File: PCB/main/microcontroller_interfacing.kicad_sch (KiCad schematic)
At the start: 20 parts, among them U3 CH340G, U4 USB_Micro_B, U5 AT24C256C-SSHL-T, X1 12MHz Crystal

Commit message: Add USB footprint
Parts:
- U4: footprint Footprint_EEE3088F:MICRO-USB-SMD_U254-051T-4BH83-S1S -> Footprint_EEE3088F:C404969_Micro_USB
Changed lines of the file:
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@@
     (property "Reference" "U4" (id 0) (at 140.97 33.181 0))
     (property "Value" "USB_Micro_B" (id 1) (at 140.97 35.7179 0))
-    (property "Footprint" "Footprint_EEE3088F:MICRO-USB-SMD_U254-051T-4BH83-S1S" (id 2) (at 139.7 43.18 0)
+    (property "Footprint" "Footprint_EEE3088F:C404969_Micro_USB" (id 2) (at 139.7 43.18 0)
       (effects (font (size 1.27 1.27)) hide)
     )

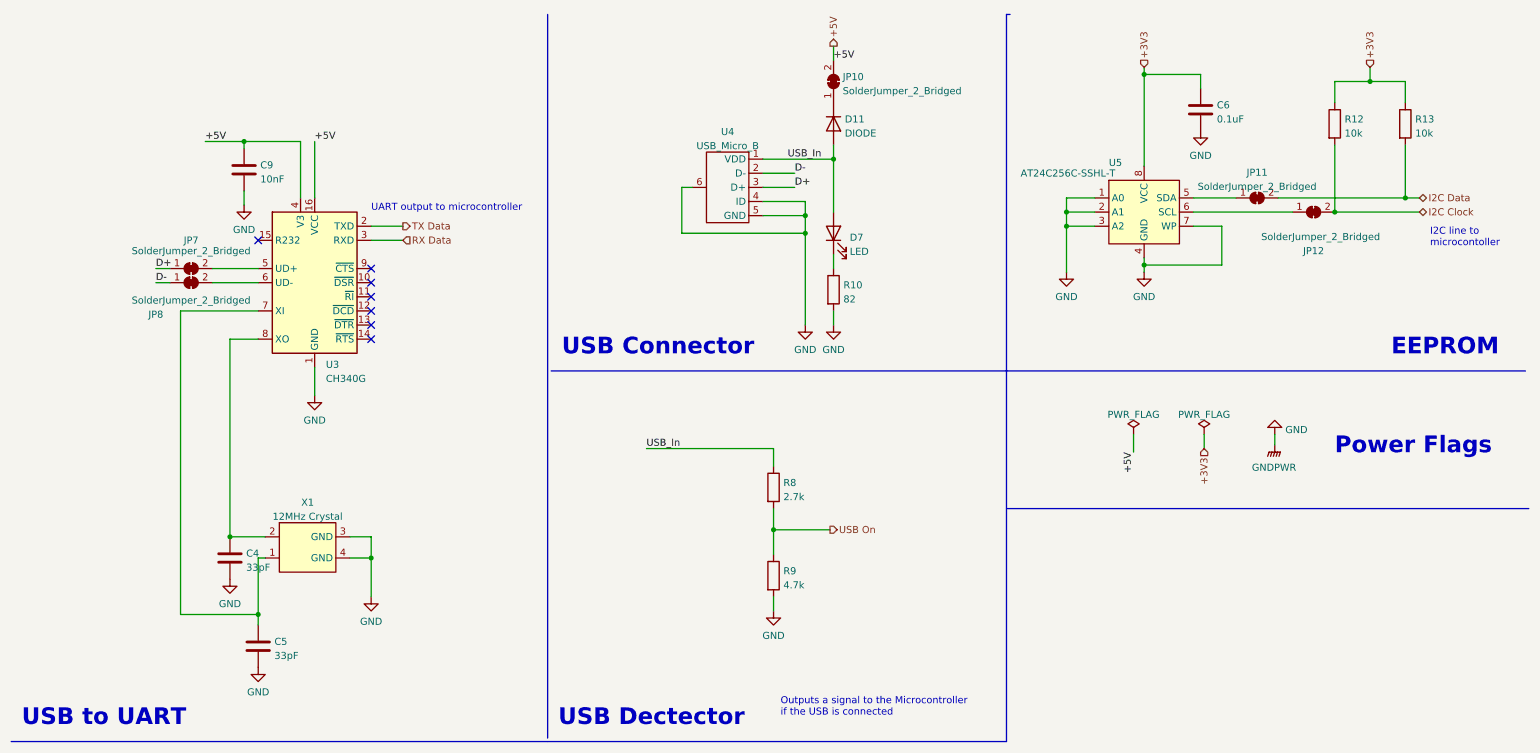
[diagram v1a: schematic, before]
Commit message: Add footprints
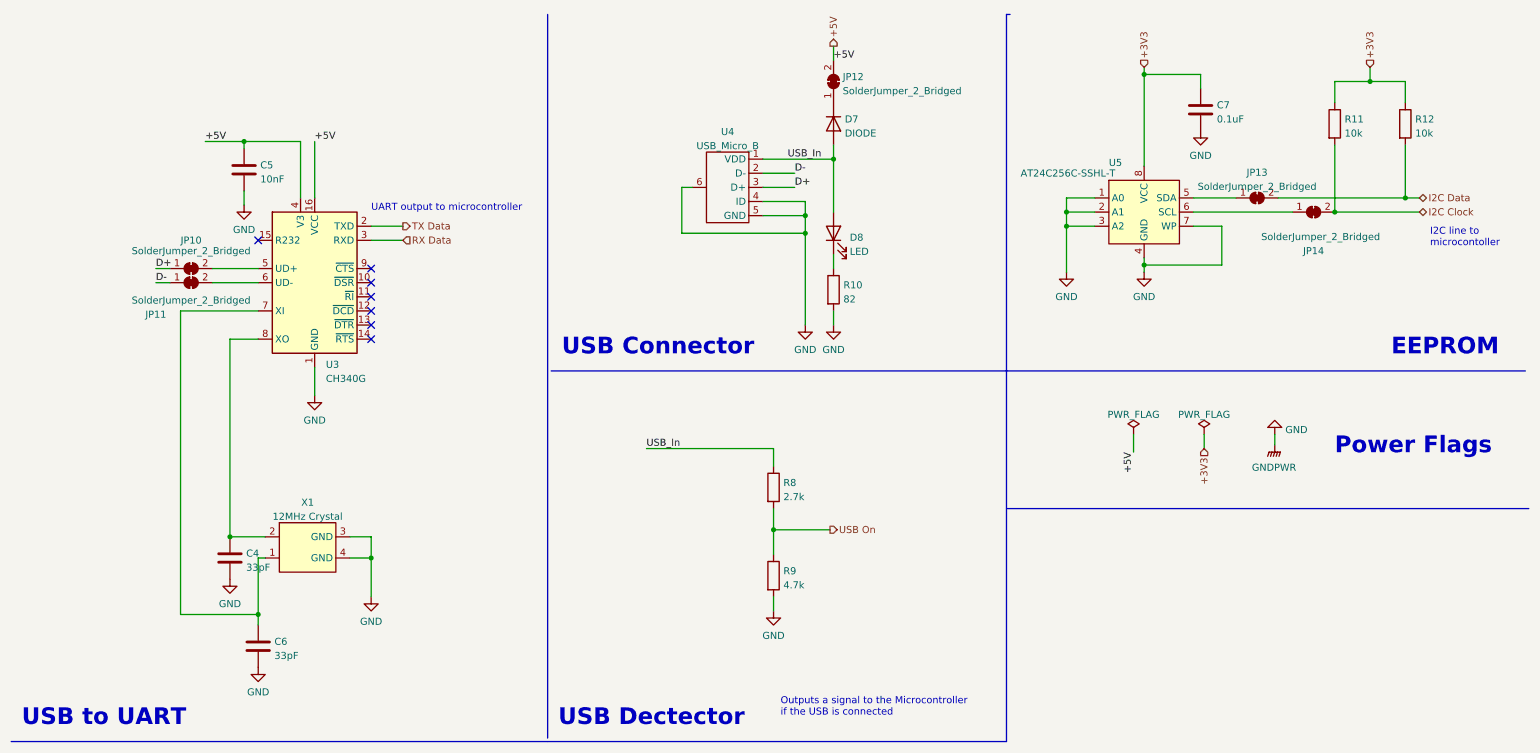
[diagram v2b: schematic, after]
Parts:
- renumbered C9 to C5, C5 to C6, C6 to C7, D11 to D7, D7 to D8, JP7 to JP10, JP8 to JP11, JP10 to JP12, JP11 to JP13, JP12 to JP14, R12 to R11, R13 to R12
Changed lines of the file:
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@@
   (symbol (lib_id "power:GND") (at 215.9 58.42 0) (unit 1)
     (in_bom yes) (on_board yes) (fields_autoplaced)
-    (property "Reference" "#PWR035" (id 0) (at 215.9 64.77 0)
+    (property "Reference" "#PWR031" (id 0) (at 215.9 64.77 0)
       (effects (font (size 1.27 1.27)) hide)
     )
@@
   (symbol (lib_id "power:GND") (at 56.515 129.54 0) (unit 1)
     (in_bom yes) (on_board yes) (fields_autoplaced)
-    (property "Reference" "#PWR026" (id 0) (at 56.515 135.89 0)
+    (property "Reference" "#PWR024" (id 0) (at 56.515 135.89 0)
       (effects (font (size 1.27 1.27)) hide)
     )
@@
   (symbol (lib_id "Jumper:SolderJumper_2_Bridged") (at 44.45 60.325 0) (unit 1)
     (in_bom yes) (on_board yes)
-    (property "Reference" "JP8" (id 0) (at 38.1 66.04 0))
+    (property "Reference" "JP11" (id 0) (at 38.1 66.04 0))
     (property "Value" "SolderJumper_2_Bridged" (id 1) (at 44.45 63.5 0))
     (property "Footprint" "Jumper:SolderJumper-2_P1.3mm_Bridged2Bar_Pad1.0x1.5mm" (id 2) (at 44.45 60.325 0)
@@
   (symbol (lib_id "power:PWR_FLAG") (at 213.995 87.63 0) (unit 1)
     (in_bom yes) (on_board yes) (fields_autoplaced)
-    (property "Reference" "#FLG01" (id 0) (at 213.995 85.725 0)
+    (property "Reference" "#FLG02" (id 0) (at 213.995 85.725 0)
       (effects (font (size 1.27 1.27)) hide)
     )
@@
   (symbol (lib_id "Device:C") (at 226.06 29.21 0) (unit 1)
     (in_bom yes) (on_board yes) (fields_autoplaced)
-    (property "Reference" "C6" (id 0) (at 228.981 28.3753 0)
+    (property "Reference" "C7" (id 0) (at 228.981 28.3753 0)
       (effects (font (size 1.27 1.27)) (justify left))
     )
@@
   (symbol (lib_id "power:GND") (at 226.06 33.02 0) (unit 1)
     (in_bom yes) (on_board yes) (fields_autoplaced)
-    (property "Reference" "#PWR03" (id 0) (at 226.06 39.37 0)
+    (property "Reference" "#PWR032" (id 0) (at 226.06 39.37 0)
       (effects (font (size 1.27 1.27)) hide)
     )
@@
   (symbol (lib_id "Jumper:SolderJumper_2_Bridged") (at 44.45 57.785 0) (unit 1)
     (in_bom yes) (on_board yes)
-    (property "Reference" "JP7" (id 0) (at 44.45 52.705 0))
+    (property "Reference" "JP10" (id 0) (at 44.45 52.705 0))
     (property "Value" "SolderJumper_2_Bridged" (id 1) (at 44.45 54.61 0))
     (property "Footprint" "Jumper:SolderJumper-2_P1.3mm_Bridged2Bar_Pad1.0x1.5mm" (id 2) (at 44.45 57.785 0)
@@
   (symbol (lib_id "Simulation_SPICE:DIODE") (at 160.02 31.75 90) (unit 1)
     (in_bom yes) (on_board yes) (fields_autoplaced)
-    (property "Reference" "D11" (id 0) (at 162.052 30.9153 90)
+    (property "Reference" "D7" (id 0) (at 162.052 30.9153 90)
       (effects (font (size 1.27 1.27)) (justify right))
     )
@@
   (symbol (lib_id "Device:R") (at 262.89 31.75 0) (unit 1)
     (in_bom yes) (on_board yes) (fields_autoplaced)
-    (property "Reference" "R13" (id 0) (at 264.668 30.9153 0)
+    (property "Reference" "R12" (id 0) (at 264.668 30.9153 0)
       (effects (font (size 1.27 1.27)) (justify left))
     )
@@
   (symbol (lib_id "Device:R") (at 250.19 31.75 0) (unit 1)
     (in_bom yes) (on_board yes) (fields_autoplaced)
-    (property "Reference" "R12" (id 0) (at 251.968 30.9153 0)
+    (property "Reference" "R11" (id 0) (at 251.968 30.9153 0)
       (effects (font (size 1.27 1.27)) (justify left))
     )
@@
   (symbol (lib_id "power:GND") (at 76.835 116.84 0) (unit 1)
     (in_bom yes) (on_board yes) (fields_autoplaced)
-    (property "Reference" "#PWR028" (id 0) (at 76.835 123.19 0)
+    (property "Reference" "#PWR026" (id 0) (at 76.835 123.19 0)
       (effects (font (size 1.27 1.27)) hide)
     )
@@
   (symbol (lib_id "Device:C") (at 53.975 40.005 0) (unit 1)
     (in_bom yes) (on_board yes) (fields_autoplaced)
-    (property "Reference" "C9" (id 0) (at 56.896 39.1703 0)
+    (property "Reference" "C5" (id 0) (at 56.896 39.1703 0)
       (effects (font (size 1.27 1.27)) (justify left))
     )
@@
   (symbol (lib_id "power:GND") (at 66.675 80.645 0) (unit 1)
     (in_bom yes) (on_board yes) (fields_autoplaced)
-    (property "Reference" "#PWR027" (id 0) (at 66.675 86.995 0)
+    (property "Reference" "#PWR025" (id 0) (at 66.675 86.995 0)
       (effects (font (size 1.27 1.27)) hide)
     )
@@
   (symbol (lib_id "power:GNDPWR") (at 239.395 89.535 0) (unit 1)
     (in_bom yes) (on_board yes) (fields_autoplaced)
-    (property "Reference" "#PWR08" (id 0) (at 239.395 94.615 0)
+    (property "Reference" "#PWR034" (id 0) (at 239.395 94.615 0)
       (effects (font (size 1.27 1.27)) hide)
     )
@@
   (symbol (lib_id "power:GND") (at 154.94 67.945 0) (unit 1)
     (in_bom yes) (on_board yes) (fields_autoplaced)
-    (property "Reference" "#PWR031" (id 0) (at 154.94 74.295 0)
+    (property "Reference" "#PWR028" (id 0) (at 154.94 74.295 0)
       (effects (font (size 1.27 1.27)) hide)
     )
@@
   (symbol (lib_id "power:GND") (at 53.975 46.355 0) (unit 1)
     (in_bom yes) (on_board yes) (fields_autoplaced)
-    (property "Reference" "#PWR02" (id 0) (at 53.975 52.705 0)
+    (property "Reference" "#PWR023" (id 0) (at 53.975 52.705 0)
       (effects (font (size 1.27 1.27)) hide)
     )
@@
   (symbol (lib_id "power:GND") (at 239.395 87.63 180) (unit 1)
     (in_bom yes) (on_board yes) (fields_autoplaced)
-    (property "Reference" "#PWR04" (id 0) (at 239.395 81.28 0)
+    (property "Reference" "#PWR033" (id 0) (at 239.395 81.28 0)
       (effects (font (size 1.27 1.27)) hide)
     )
@@
   (symbol (lib_id "power:PWR_FLAG") (at 226.695 87.63 0) (unit 1)
     (in_bom yes) (on_board yes) (fields_autoplaced)
-    (property "Reference" "#FLG02" (id 0) (at 226.695 85.725 0)
+    (property "Reference" "#FLG03" (id 0) (at 226.695 85.725 0)
       (effects (font (size 1.27 1.27)) hide)
     )
@@
   (symbol (lib_id "power:GND") (at 51.435 113.665 0) (unit 1)
     (in_bom yes) (on_board yes) (fields_autoplaced)
-    (property "Reference" "#PWR025" (id 0) (at 51.435 120.015 0)
+    (property "Reference" "#PWR022" (id 0) (at 51.435 120.015 0)
       (effects (font (size 1.27 1.27)) hide)
     )
@@
   (symbol (lib_id "Device:C") (at 56.515 125.73 0) (unit 1)
     (in_bom yes) (on_board yes) (fields_autoplaced)
-    (property "Reference" "C5" (id 0) (at 59.436 124.8953 0)
+    (property "Reference" "C6" (id 0) (at 59.436 124.8953 0)
       (effects (font (size 1.27 1.27)) (justify left))
     )
@@
   (symbol (lib_id "power:GND") (at 160.02 67.945 0) (unit 1)
     (in_bom yes) (on_board yes) (fields_autoplaced)
-    (property "Reference" "#PWR032" (id 0) (at 160.02 74.295 0)
+    (property "Reference" "#PWR029" (id 0) (at 160.02 74.295 0)
       (effects (font (size 1.27 1.27)) hide)
     )
@@
   (symbol (lib_id "Jumper:SolderJumper_2_Bridged") (at 160.02 24.13 90) (unit 1)
     (in_bom yes) (on_board yes) (fields_autoplaced)
-    (property "Reference" "JP10" (id 0) (at 161.671 23.2953 90)
+    (property "Reference" "JP12" (id 0) (at 161.671 23.2953 90)
       (effects (font (size 1.27 1.27)) (justify right))
     )
@@
   (symbol (lib_id "Jumper:SolderJumper_2_Bridged") (at 246.38 47.625 0) (unit 1)
     (in_bom yes) (on_board yes)
-    (property "Reference" "JP12" (id 0) (at 246.38 54.61 0))
+    (property "Reference" "JP14" (id 0) (at 246.38 54.61 0))
     (property "Value" "SolderJumper_2_Bridged" (id 1) (at 247.65 52.07 0))
     (property "Footprint" "Jumper:SolderJumper-2_P1.3mm_Bridged2Bar_Pad1.0x1.5mm" (id 2) (at 246.38 47.625 0)
@@
   (symbol (lib_id "power:GND") (at 149.225 119.38 0) (unit 1)
     (in_bom yes) (on_board yes) (fields_autoplaced)
-    (property "Reference" "#PWR029" (id 0) (at 149.225 125.73 0)
+    (property "Reference" "#PWR027" (id 0) (at 149.225 125.73 0)
       (effects (font (size 1.27 1.27)) hide)
     )
@@
   (symbol (lib_id "Jumper:SolderJumper_2_Bridged") (at 236.22 45.085 0) (unit 1)
     (in_bom yes) (on_board yes) (fields_autoplaced)
-    (property "Reference" "JP11" (id 0) (at 236.22 40.4962 0))
+    (property "Reference" "JP13" (id 0) (at 236.22 40.4962 0))
     (property "Value" "SolderJumper_2_Bridged" (id 1) (at 236.22 43.0331 0))
     (property "Footprint" "Jumper:SolderJumper-2_P1.3mm_Bridged2Bar_Pad1.0x1.5mm" (id 2) (at 236.22 45.085 0)
@@
   (symbol (lib_id "power:GND") (at 201.93 58.42 0) (unit 1)
     (in_bom yes) (on_board yes) (fields_autoplaced)
-    (property "Reference" "#PWR034" (id 0) (at 201.93 64.77 0)
+    (property "Reference" "#PWR030" (id 0) (at 201.93 64.77 0)
       (effects (font (size 1.27 1.27)) hide)
     )
@@
   (symbol (lib_id "Device:LED") (at 160.02 51.435 90) (unit 1)
     (in_bom yes) (on_board yes) (fields_autoplaced)
-    (property "Reference" "D7" (id 0) (at 162.941 52.1878 90)
+    (property "Reference" "D8" (id 0) (at 162.941 52.1878 90)
       (effects (font (size 1.27 1.27)) (justify right))
     )

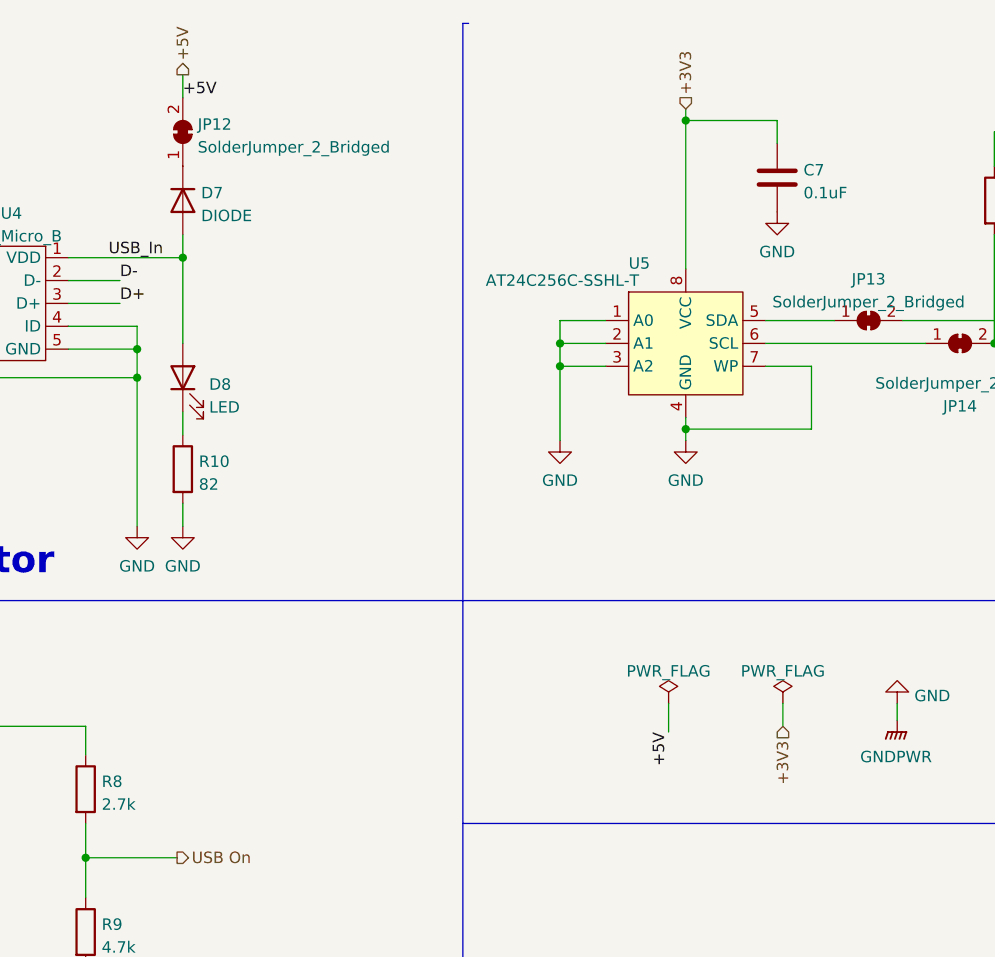
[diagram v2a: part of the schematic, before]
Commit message: Add voltage regulator
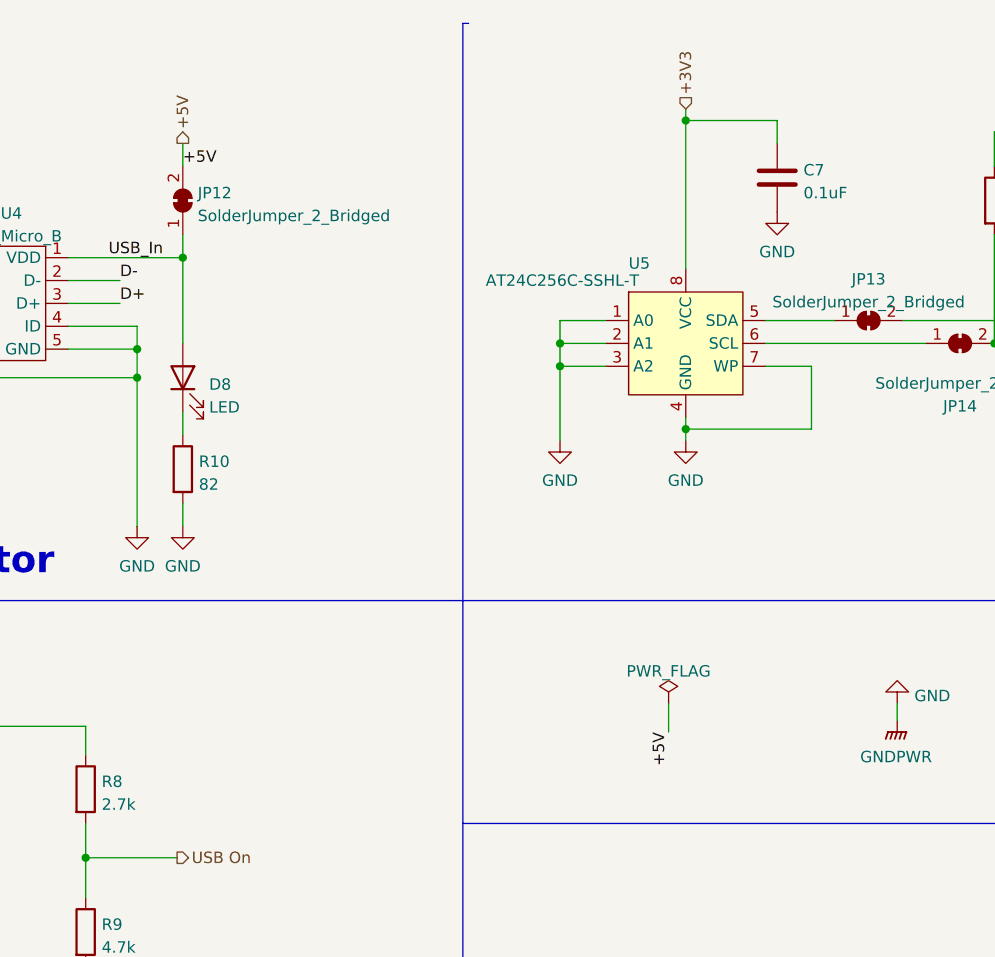
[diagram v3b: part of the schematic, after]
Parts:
- removed D7: DIODE, Diode_SMD:D_SMA, symbol Simulation_SPICE:DIODE
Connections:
- net USB_In: now also JP12.1 (A)
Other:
- moved on the sheet: JP12
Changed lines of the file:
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@@
     (stroke (width 0) (type default) (color 0 0 0 0))
   )
-  (wire (pts (xy 160.02 17.78) (xy 160.02 20.32))
+  (wire (pts (xy 160.02 25.4) (xy 160.02 27.94))
     (stroke (width 0) (type default) (color 0 0 0 0))
   )
@@
   )
   (polyline (pts (xy 109.22 76.2) (xy 284.48 76.2))
-    (stroke (width 0) (type default) (color 0 0 0 0))
-  )
-  (wire (pts (xy 226.695 87.63) (xy 226.695 90.17))
     (stroke (width 0) (type default) (color 0 0 0 0))
   )
@@
     (effects (font (size 1.27 1.27)) (justify left bottom))
   )
-  (label "+5V" (at 160.02 20.32 0)
+  (label "+5V" (at 160.02 27.94 0)
     (effects (font (size 1.27 1.27)) (justify left bottom))
   )
@@
     (effects (font (size 1.27 1.27)) (justify left))
   )
-  (hierarchical_label "+5V" (shape output) (at 160.02 17.78 90)
+  (hierarchical_label "+5V" (shape output) (at 160.02 25.4 90)
     (effects (font (size 1.27 1.27)) (justify left))
   )
@@
   (hierarchical_label "TX Data" (shape output) (at 82.55 50.165 0)
     (effects (font (size 1.27 1.27)) (justify left))
-  )
-  (hierarchical_label "+3V3" (shape input) (at 226.695 90.17 270)
-    (effects (font (size 1.27 1.27)) (justify right))
   )
   (symbol (lib_id "power:GND") (at 215.9 58.42 0) (unit 1)
@@
     (pin "2")
   )
-  (symbol (lib_id "Simulation_SPICE:DIODE") (at 160.02 31.75 90) (unit 1)
-    (in_bom yes) (on_board yes) (fields_autoplaced)
-    (property "Reference" "D7" (id 0) (at 162.052 30.9153 90)
-      (effects (font (size 1.27 1.27)) (justify right))
-    )
-    (property "Value" "DIODE" (id 1) (at 162.052 33.4522 90)
-      (effects (font (size 1.27 1.27)) (justify right))
-    )
-    (property "Footprint" "Diode_SMD:D_SMA" (id 2) (at 160.02 31.75 0)
-      (effects (font (size 1.27 1.27)) hide)
-    )
-    (property "Datasheet" "~" (id 3) (at 160.02 31.75 0)
-      (effects (font (size 1.27 1.27)) hide)
-    )
-    (property "Spice_Netlist_Enabled" "Y" (id 4) (at 160.02 31.75 0)
-      (effects (font (size 1.27 1.27)) (justify left) hide)
-    )
-    (property "Spice_Primitive" "D" (id 5) (at 160.02 31.75 0)
-      (effects (font (size 1.27 1.27)) (justify left) hide)
-    )
-    (pin "1")
-    (pin "2")
-  )
   (symbol (lib_id "Device:R") (at 262.89 31.75 0) (unit 1)
     (in_bom yes) (on_board yes) (fields_autoplaced)
@@
     )
     (property "Datasheet" "" (id 3) (at 239.395 87.63 0)
-      (effects (font (size 1.27 1.27)) hide)
-    )
-    (pin "1")
-  )
-  (symbol (lib_id "power:PWR_FLAG") (at 226.695 87.63 0) (unit 1)
-    (in_bom yes) (on_board yes) (fields_autoplaced)
-    (property "Reference" "#FLG03" (id 0) (at 226.695 85.725 0)
-      (effects (font (size 1.27 1.27)) hide)
-    )
-    (property "Value" "PWR_FLAG" (id 1) (at 226.695 84.0542 0))
-    (property "Footprint" "" (id 2) (at 226.695 87.63 0)
-      (effects (font (size 1.27 1.27)) hide)
-    )
-    (property "Datasheet" "~" (id 3) (at 226.695 87.63 0)
       (effects (font (size 1.27 1.27)) hide)
     )
@@
     (pin "1")
   )
-  (symbol (lib_id "Jumper:SolderJumper_2_Bridged") (at 160.02 24.13 90) (unit 1)
-    (in_bom yes) (on_board yes) (fields_autoplaced)
-    (property "Reference" "JP12" (id 0) (at 161.671 23.2953 90)
+  (symbol (lib_id "Jumper:SolderJumper_2_Bridged") (at 160.02 31.75 90) (unit 1)
+    (in_bom yes) (on_board yes) (fields_autoplaced)
+    (property "Reference" "JP12" (id 0) (at 161.671 30.9153 90)
       (effects (font (size 1.27 1.27)) (justify right))
     )
-    (property "Value" "SolderJumper_2_Bridged" (id 1) (at 161.671 25.8322 90)
+    (property "Value" "SolderJumper_2_Bridged" (id 1) (at 161.671 33.4522 90)
       (effects (font (size 1.27 1.27)) (justify right))
     )
-    (property "Footprint" "Jumper:SolderJumper-2_P1.3mm_Bridged2Bar_Pad1.0x1.5mm" (id 2) (at 160.02 24.13 0)
-      (effects (font (size 1.27 1.27)) hide)
-    )
-    (property "Datasheet" "~" (id 3) (at 160.02 24.13 0)
-      (effects (font (size 1.27 1.27)) hide)
-    )
+    (property "Footprint" "Jumper:SolderJumper-2_P1.3mm_Bridged2Bar_Pad1.0x1.5mm" (id 2) (at 160.02 31.75 0)
+      (effects (font (size 1.27 1.27)) hide)
+    )
+    (property "Datasheet" "~" (id 3) (at 160.02 31.75 0)
+      (effects (font (size 1.27 1.27)) hide)
+    )
